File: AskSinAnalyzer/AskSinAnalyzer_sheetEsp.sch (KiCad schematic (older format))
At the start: 14 parts, among them J11 FTDI_ESP, SW11 DIP4, SW12 Flash, SW13 Button, U11 TJCTM24028-SPI, U12 ESP-WROOM-32

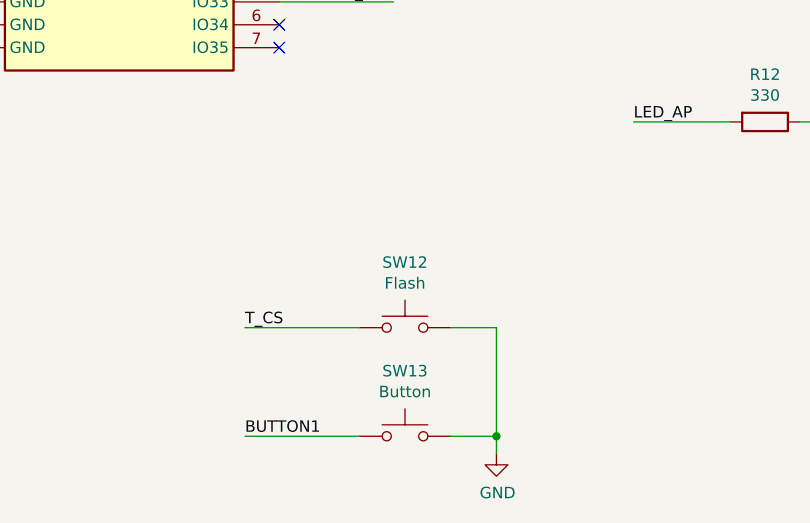
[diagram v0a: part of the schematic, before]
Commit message: PCB update
reference labels moved
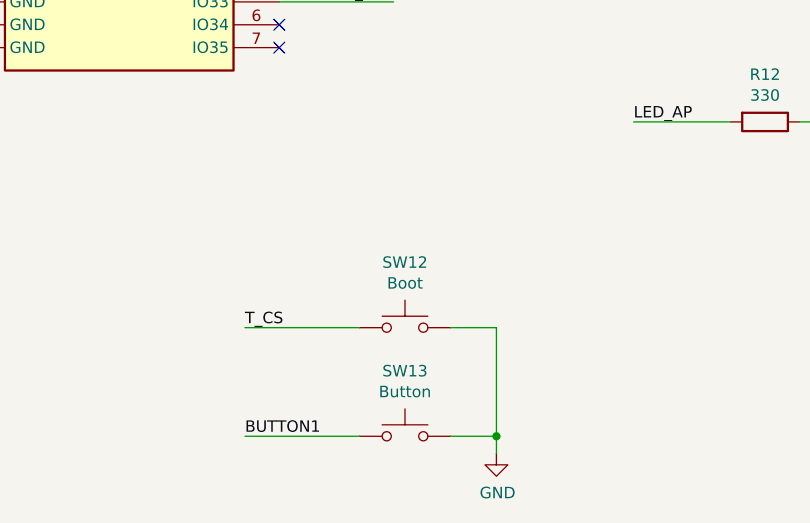
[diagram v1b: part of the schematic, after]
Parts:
- SW12: value Flash -> Boot
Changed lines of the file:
@@
 AR Path="/5D4B4DC0/5D50C20D" Ref="SW12"  Part="1"
 F 0 "SW12" H 5550 6585 50  0000 C CNN
-F 1 "Flash" H 5550 6494 50  0000 C CNN
+F 1 "Boot" H 5550 6494 50  0000 C CNN
 F 2 "Buttons_Switches_THT:SW_PUSH_6mm" H 5550 6500 50  0001 C CNN
 F 3 "~" H 5550 6500 50  0001 C CNN

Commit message: PCB update
pads for ESP made longer
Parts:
- U12: footprint myEspModules:ESP-WROOM-32 -> myEspModules:ESP-WROOM-32_handsoldering
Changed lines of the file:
@@
 F 0 "U12" H 4300 5342 50  0000 C CNN
 F 1 "ESP-WROOM-32" H 4300 5251 50  0000 C CNN
-F 2 "myEspModules:ESP-WROOM-32" H 4300 2375 50  0001 C CNN
+F 2 "myEspModules:ESP-WROOM-32_handsoldering" H 4300 2375 50  0001 C CNN
 F 3 "https://www.espressif.com/sites/default/files/documentation/esp32-wroom-32_datasheet_en.pdf" H 4000 3925 50  0001 C CNN
 	1    4300 3875

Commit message: AskSinAnalyzer PCB V2.0 RC1
added a FTDI FT245 to flash and debug ESP32
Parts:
- added Q11, Q12: BC817, TO_SOT_Packages_SMD:SOT-23_Handsoldering, symbol Transistor_BJT:BC817
- added R13, R14: 10k, Resistors_SMD:R_0805_HandSoldering, symbol Device:R
- added SW14: Reset, Buttons_Switches_THT:SW_PUSH_6mm, symbol Switch:SW_Push
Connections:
- net RX is gone; now on net ESP_RX: J11.3 (TX), U12.34 (RXD0/IO3)
- net TX is gone; now on net ESP_TX: J11.2 (RX), U12.35 (TXD0/IO1)
- net EN: now also Q12.3 (C), SW14.1
- net ESP_RX: no longer U12.27 (IO16)
- net ESP_TX: no longer U12.28 (IO17)
- net GND: now also SW14.2
- net T_CS: now also Q11.3 (C)
- new net: Q11.1 (B), R13.1
- new net: Q12.1 (B), R14.1
- new net ESP_DTR: Q11.2 (E), R14.2
- new net ESP_RTS: Q12.2 (E), R13.2
- new net ESP_RX2: U12.27 (IO16)
- new net ESP_TX2: U12.28 (IO17)
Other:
- moved on the sheet: J11, SW12, SW13
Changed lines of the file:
@@
 Wire Wire Line
 	3450 4975 3450 5075
-Wire Wire Line
-	5000 3025 5500 3025
-Wire Wire Line
-	5500 2825 5000 2825
 Text Label 5500 2825 2    50   ~ 0
 TX
@@
 L myConnectors:FtdiConnector J?
 U 1 1 5D4D5F4D
-P 2625 6450
+P 1200 6475
 AR Path="/5D4D5F4D" Ref="J?"  Part="1"
 AR Path="/5D4B4DC0/5D4D5F4D" Ref="J11"  Part="1"
-F 0 "J11" H 3153 6526 50  0000 L CNN
-F 1 "FTDI_ESP" H 3153 6435 50  0000 L CNN
-F 2 "myPinHeaders:Pin_Header_Straight_1x06_Pitch2.54mm_Tight_Fit" H 2625 6450 50  0001 C CNN
-F 3 "" H 2625 6450 50  0001 C CNN
-	1    2625 6450
-	1    0    0    -1
-$EndComp
-Wire Wire Line
-	2225 6350 2625 6350
+F 0 "J11" H 1728 6551 50  0000 L CNN
+F 1 "FTDI_ESP" H 1728 6460 50  0000 L CNN
+F 2 "myPinHeaders:Pin_Header_Straight_1x06_Pitch2.54mm_Tight_Fit" H 1200 6475 50  0001 C CNN
+F 3 "" H 1200 6475 50  0001 C CNN
+	1    1200 6475
+	1    0    0    -1
+$EndComp
+Wire Wire Line
+	800  6375 1200 6375
 $Comp
 L power:GND #PWR?
 U 1 1 5D4D5F54
-P 2550 6825
+P 1125 6850
 AR Path="/5D4D5F54" Ref="#PWR?"  Part="1"
 AR Path="/5D4B4DC0/5D4D5F54" Ref="#PWR028"  Part="1"
-F 0 "#PWR028" H 2550 6575 50  0001 C CNN
-F 1 "GND" H 2555 6652 50  0000 C CNN
-F 2 "" H 2550 6825 50  0001 C CNN
-F 3 "" H 2550 6825 50  0001 C CNN
-	1    2550 6825
-	1    0    0    -1
-$EndComp
-Wire Wire Line
-	2550 6825 2550 6750
-Wire Wire Line
-	2550 6750 2625 6750
-Wire Wire Line
-	2625 6250 2225 6250
-NoConn ~ 2625 6500
-NoConn ~ 2625 6600
+F 0 "#PWR028" H 1125 6600 50  0001 C CNN
+F 1 "GND" H 1130 6677 50  0000 C CNN
+F 2 "" H 1125 6850 50  0001 C CNN
+F 3 "" H 1125 6850 50  0001 C CNN
+	1    1125 6850
+	1    0    0    -1
+$EndComp
+Wire Wire Line
+	1125 6850 1125 6775
+Wire Wire Line
+	1125 6775 1200 6775
+Wire Wire Line
+	1200 6275 800  6275
+NoConn ~ 1200 6525
+NoConn ~ 1200 6625
 $Comp
 L power:+3.3V #PWR?
 U 1 1 5D4D5F5F
-P 2525 6025
+P 1100 6050
 AR Path="/5D4D5F5F" Ref="#PWR?"  Part="1"
 AR Path="/5D4B4DC0/5D4D5F5F" Ref="#PWR027"  Part="1"
-F 0 "#PWR027" H 2525 5875 50  0001 C CNN
-F 1 "+3.3V" H 2540 6198 50  0000 C CNN
-F 2 "" H 2525 6025 50  0001 C CNN
-F 3 "" H 2525 6025 50  0001 C CNN
-	1    2525 6025
-	1    0    0    -1
-$EndComp
-Wire Wire Line
-	2525 6025 2525 6100
-Wire Wire Line
-	2525 6100 2625 6100
-Text Label 2225 6250 0    50   ~ 0
+F 0 "#PWR027" H 1100 5900 50  0001 C CNN
+F 1 "+3.3V" H 1115 6223 50  0000 C CNN
+F 2 "" H 1100 6050 50  0001 C CNN
+F 3 "" H 1100 6050 50  0001 C CNN
+	1    1100 6050
+	1    0    0    -1
+$EndComp
+Wire Wire Line
+	1100 6050 1100 6125
+Wire Wire Line
+	1100 6125 1200 6125
+Text Label 800  6275 0    50   ~ 0
 TX
-Text Label 2225 6350 0    50   ~ 0
+Text Label 800  6375 0    50   ~ 0
 RX
 $Comp
@@
 L Switch:SW_Push SW?
 U 1 1 5D5050FA
-P 5550 6775
+P 6100 7075
 AR Path="/5D5050FA" Ref="SW?"  Part="1"
 AR Path="/5D4B4DC0/5D5050FA" Ref="SW13"  Part="1"
-F 0 "SW13" H 5550 7060 50  0000 C CNN
-F 1 "Button" H 5550 6969 50  0000 C CNN
-F 2 "Buttons_Switches_THT:SW_PUSH_6mm" H 5550 6975 50  0001 C CNN
-F 3 "~" H 5550 6975 50  0001 C CNN
-	1    5550 6775
-	1    0    0    -1
-$EndComp
-Text Label 4850 6775 0    50   ~ 0
+F 0 "SW13" H 6100 7360 50  0000 C CNN
+F 1 "Button" H 6100 7269 50  0000 C CNN
+F 2 "Buttons_Switches_THT:SW_PUSH_6mm" H 6100 7275 50  0001 C CNN
+F 3 "~" H 6100 7275 50  0001 C CNN
+	1    6100 7075
+	1    0    0    -1
+$EndComp
+Text Label 5400 7075 0    50   ~ 0
 BUTTON1
 Wire Wire Line
-	4850 6775 5350 6775
+	5400 7075 5900 7075
 $Comp
 L power:GND #PWR?
 U 1 1 5D505102
-P 5950 6850
+P 6500 7150
 AR Path="/5D505102" Ref="#PWR?"  Part="1"
 AR Path="/5D4B4DC0/5D505102" Ref="#PWR029"  Part="1"
-F 0 "#PWR029" H 5950 6600 50  0001 C CNN
-F 1 "GND" H 5955 6677 50  0000 C CNN
-F 2 "" H 5950 6850 50  0001 C CNN
-F 3 "" H 5950 6850 50  0001 C CNN
-	1    5950 6850
-	1    0    0    -1
-$EndComp
-Wire Wire Line
-	5950 6850 5950 6775
-Wire Wire Line
-	5950 6775 5750 6775
+F 0 "#PWR029" H 6500 6900 50  0001 C CNN
+F 1 "GND" H 6505 6977 50  0000 C CNN
+F 2 "" H 6500 7150 50  0001 C CNN
+F 3 "" H 6500 7150 50  0001 C CNN
+	1    6500 7150
+	1    0    0    -1
+$EndComp
+Wire Wire Line
+	6500 7150 6500 7075
+Wire Wire Line
+	6500 7075 6300 7075
 Wire Wire Line
 	5000 2725 5500 2725
@@
 L Switch:SW_Push SW?
 U 1 1 5D50C20D
-P 5550 6300
+P 6100 6600
 AR Path="/5D50C20D" Ref="SW?"  Part="1"
 AR Path="/5D4B4DC0/5D50C20D" Ref="SW12"  Part="1"
-F 0 "SW12" H 5550 6585 50  0000 C CNN
-F 1 "Boot" H 5550 6494 50  0000 C CNN
-F 2 "Buttons_Switches_THT:SW_PUSH_6mm" H 5550 6500 50  0001 C CNN
-F 3 "~" H 5550 6500 50  0001 C CNN
-	1    5550 6300
-	1    0    0    -1
-$EndComp
-Wire Wire Line
-	5750 6300 5950 6300
-Wire Wire Line
-	5950 6300 5950 6775
-Connection ~ 5950 6775
-Wire Wire Line
-	5350 6300 4850 6300
-Text Label 4850 6300 0    50   ~ 0
+F 0 "SW12" H 6100 6885 50  0000 C CNN
+F 1 "Boot" H 6100 6794 50  0000 C CNN
+F 2 "Buttons_Switches_THT:SW_PUSH_6mm" H 6100 6800 50  0001 C CNN
+F 3 "~" H 6100 6800 50  0001 C CNN
+	1    6100 6600
+	1    0    0    -1
+$EndComp
+Wire Wire Line
+	6300 6600 6500 6600
+Wire Wire Line
+	6500 6600 6500 7075
+Connection ~ 6500 7075
+Wire Wire Line
+	5900 6600 5400 6600
+Text Label 5400 6600 0    50   ~ 0
 T_CS
 $Comp
@@
 	8675 950  8675 1100
 Text HLabel 5650 3775 2    50   Input ~ 0
-ESP_RX
+ESP_RX2
 Text HLabel 5650 3875 2    50   Input ~ 0
-ESP_TX
+ESP_TX2
 Wire Wire Line
 	10050 3450 9450 3450
@@
 Text Label 3450 3025 0    50   ~ 0
 EN
+$Comp
+L Switch:SW_Push SW?
+U 1 1 5D60F4D4
+P 6100 6125
+AR Path="/5D60F4D4" Ref="SW?"  Part="1"
+AR Path="/5D4B4DC0/5D60F4D4" Ref="SW14"  Part="1"
+F 0 "SW14" H 6100 6410 50  0000 C CNN
+F 1 "Reset" H 6100 6319 50  0000 C CNN
+F 2 "Buttons_Switches_THT:SW_PUSH_6mm" H 6100 6325 50  0001 C CNN
+F 3 "~" H 6100 6325 50  0001 C CNN
+	1    6100 6125
+	1    0    0    -1
+$EndComp
+Wire Wire Line
+	6300 6125 6500 6125
+Wire Wire Line
+	6500 6125 6500 6600
+Connection ~ 6500 6600
+Wire Wire Line
+	5900 6125 5400 6125
+Text Label 5400 6125 0    50   ~ 0
+EN
+$Comp
+L Device:R R?
+U 1 1 5D634714
+P 3275 6150
+AR Path="/5D634714" Ref="R?"  Part="1"
+AR Path="/5D4B4DC0/5D634714" Ref="R13"  Part="1"
+F 0 "R13" V 3068 6150 50  0000 C CNN
+F 1 "10k" V 3159 6150 50  0000 C CNN
+F 2 "Resistors_SMD:R_0805_HandSoldering" V 3205 6150 50  0001 C CNN
+F 3 "~" H 3275 6150 50  0001 C CNN
+	1    3275 6150
+	0    1    1    0
+$EndComp
+$Comp
+L Device:R R?
+U 1 1 5D634C12
+P 3275 6925
+AR Path="/5D634C12" Ref="R?"  Part="1"
+AR Path="/5D4B4DC0/5D634C12" Ref="R14"  Part="1"
+F 0 "R14" V 3068 6925 50  0000 C CNN
+F 1 "10k" V 3159 6925 50  0000 C CNN
+F 2 "Resistors_SMD:R_0805_HandSoldering" V 3205 6925 50  0001 C CNN
+F 3 "~" H 3275 6925 50  0001 C CNN
+	1    3275 6925
+	0    1    1    0
+$EndComp
+Wire Wire Line
+	3425 6925 3500 6925
+Wire Wire Line
+	3425 6150 3500 6150
+Wire Wire Line
+	3125 6150 3000 6150
+Connection ~ 3000 6150
+Wire Wire Line
+	3000 6150 2825 6150
+Wire Wire Line
+	3800 6725 3800 6600
+Wire Wire Line
+	3800 6600 3150 6600
+Wire Wire Line
+	3150 6600 3000 6425
+Wire Wire Line
+	3000 6425 3000 6150
+Wire Wire Line
+	3125 6925 3000 6925
+Wire Wire Line
+	3000 6925 3000 6600
+Wire Wire Line
+	3800 6425 3800 6350
+Wire Wire Line
+	3800 6425 3150 6425
+Wire Wire Line
+	3150 6425 3000 6600
+Wire Wire Line
+	3800 7125 3800 7250
+Wire Wire Line
+	3800 7250 4250 7250
+Text Label 4250 7250 2    50   ~ 0
+EN
+Wire Wire Line
+	3800 5950 3800 5850
+Wire Wire Line
+	3800 5850 4250 5850
+Text Label 4250 5850 2    50   ~ 0
+T_CS
+Text HLabel 2825 6150 0    50   Input ~ 0
+ESP_RTS
+Text HLabel 2825 6925 0    50   Input ~ 0
+ESP_DTR
+Wire Wire Line
+	2825 6925 3000 6925
+Connection ~ 3000 6925
+$Comp
+L Transistor_BJT:BC817 Q11
+U 1 1 5D69CF68
+P 3700 6150
+F 0 "Q11" H 3891 6196 50  0000 L CNN
+F 1 "BC817" H 3891 6105 50  0000 L CNN
+F 2 "TO_SOT_Packages_SMD:SOT-23_Handsoldering" H 3900 6075 50  0001 L CIN
+F 3 "http://www.fairchildsemi.com/ds/BC/BC817.pdf" H 3700 6150 50  0001 L CNN
+	1    3700 6150
+	1    0    0    -1
+$EndComp
+$Comp
+L Transistor_BJT:BC817 Q12
+U 1 1 5D69E995
+P 3700 6925
+F 0 "Q12" H 3891 6879 50  0000 L CNN
+F 1 "BC817" H 3891 6970 50  0000 L CNN
+F 2 "TO_SOT_Packages_SMD:SOT-23_Handsoldering" H 3900 6850 50  0001 L CIN
+F 3 "http://www.fairchildsemi.com/ds/BC/BC817.pdf" H 3700 6925 50  0001 L CNN
+	1    3700 6925
+	1    0    0    1
+$EndComp
+Text HLabel 5650 3025 2    50   Input ~ 0
+ESP_RX
+Text HLabel 5650 2825 2    50   Input ~ 0
+ESP_TX
+Wire Wire Line
+	5000 3025 5650 3025
+Wire Wire Line
+	5000 2825 5650 2825
 $EndSCHEMATC

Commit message: AskSinAnalyzer PCB V2.0
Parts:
- added R15: 10k, Resistors_SMD:R_0805_HandSoldering, symbol Device:R
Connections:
- net +3V3: now also R15.1
- net T_CS: now also R15.2
- net SW_DETAIL renamed SW1_DETAIL
- net SW_LINES renamed SW3_LINES
- net SW_ONLINE renamed SW2_ONLINE
- net SW_UNUSED renamed SW4_UNUSED
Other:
- moved on the sheet: SW12, SW14
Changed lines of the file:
@@
 NoConn ~ 5000 4975
 NoConn ~ 5000 4275
-NoConn ~ 5000 4175
 NoConn ~ 3600 3625
 NoConn ~ 3600 3725
 NoConn ~ 3600 3825
 Text Label 5500 3375 2    50   ~ 0
-SW_DETAIL
+SW1_DETAIL
 Wire Wire Line
 	5500 3375 5000 3375
 Text Label 5500 3475 2    50   ~ 0
-SW_LINES
+SW3_LINES
 Text Label 5500 3575 2    50   ~ 0
-SW_ONLINE
+SW2_ONLINE
 Text Label 5500 3675 2    50   ~ 0
 BUTTON1
@@
 	5000 3125 5500 3125
 Text Label 5500 3125 2    50   ~ 0
-SW_UNUSED
+SW4_UNUSED
 $Comp
 L power:GND #PWR?
@@
 	9075 5350 8675 5350
 Text Label 8675 5350 0    50   ~ 0
-SW_DETAIL
+SW1_DETAIL
 Text Label 8675 5450 0    50   ~ 0
-SW_ONLINE
+SW2_ONLINE
 Text Label 8675 5550 0    50   ~ 0
-SW_LINES
+SW3_LINES
 Wire Wire Line
 	8675 5550 9075 5550
@@
 	9075 5650 8675 5650
 Text Label 8675 5650 0    50   ~ 0
-SW_UNUSED
+SW4_UNUSED
 Wire Wire Line
 	9675 5650 9775 5650
@@
 	6500 7075 6300 7075
 Wire Wire Line
-	5000 2725 5500 2725
+	5000 2725 5250 2725
 Text Label 5500 2725 2    50   ~ 0
 T_CS
@@
 L Switch:SW_Push SW?
 U 1 1 5D50C20D
-P 6100 6600
+P 6100 6125
 AR Path="/5D50C20D" Ref="SW?"  Part="1"
 AR Path="/5D4B4DC0/5D50C20D" Ref="SW12"  Part="1"
-F 0 "SW12" H 6100 6885 50  0000 C CNN
-F 1 "Boot" H 6100 6794 50  0000 C CNN
-F 2 "Buttons_Switches_THT:SW_PUSH_6mm" H 6100 6800 50  0001 C CNN
-F 3 "~" H 6100 6800 50  0001 C CNN
-	1    6100 6600
-	1    0    0    -1
-$EndComp
-Wire Wire Line
-	6300 6600 6500 6600
-Wire Wire Line
-	6500 6600 6500 7075
+F 0 "SW12" H 6100 6410 50  0000 C CNN
+F 1 "Boot" H 6100 6319 50  0000 C CNN
+F 2 "Buttons_Switches_THT:SW_PUSH_6mm" H 6100 6325 50  0001 C CNN
+F 3 "~" H 6100 6325 50  0001 C CNN
+	1    6100 6125
+	1    0    0    -1
+$EndComp
+Wire Wire Line
+	6300 6125 6500 6125
 Connection ~ 6500 7075
-Wire Wire Line
-	5900 6600 5400 6600
-Text Label 5400 6600 0    50   ~ 0
+Text Label 5400 6125 0    50   ~ 0
 T_CS
 $Comp
@@
 L Switch:SW_Push SW?
 U 1 1 5D60F4D4
-P 6100 6125
+P 6100 6625
 AR Path="/5D60F4D4" Ref="SW?"  Part="1"
 AR Path="/5D4B4DC0/5D60F4D4" Ref="SW14"  Part="1"
-F 0 "SW14" H 6100 6410 50  0000 C CNN
-F 1 "Reset" H 6100 6319 50  0000 C CNN
-F 2 "Buttons_Switches_THT:SW_PUSH_6mm" H 6100 6325 50  0001 C CNN
-F 3 "~" H 6100 6325 50  0001 C CNN
-	1    6100 6125
-	1    0    0    -1
-$EndComp
-Wire Wire Line
-	6300 6125 6500 6125
-Wire Wire Line
-	6500 6125 6500 6600
-Connection ~ 6500 6600
-Wire Wire Line
-	5900 6125 5400 6125
-Text Label 5400 6125 0    50   ~ 0
+F 0 "SW14" H 6100 6910 50  0000 C CNN
+F 1 "Reset" H 6100 6819 50  0000 C CNN
+F 2 "Buttons_Switches_THT:SW_PUSH_6mm" H 6100 6825 50  0001 C CNN
+F 3 "~" H 6100 6825 50  0001 C CNN
+	1    6100 6625
+	1    0    0    -1
+$EndComp
+Wire Wire Line
+	6300 6625 6500 6625
+Wire Wire Line
+	5900 6625 5400 6625
+Text Label 5400 6625 0    50   ~ 0
 EN
 $Comp
@@
 Text HLabel 2825 6150 0    50   Input ~ 0
 ESP_RTS
-Text HLabel 2825 6925 0    50   Input ~ 0
-ESP_DTR
-Wire Wire Line
-	2825 6925 3000 6925
-Connection ~ 3000 6925
 $Comp
 L Transistor_BJT:BC817 Q11
@@
 Wire Wire Line
 	5000 2825 5650 2825
+NoConn ~ 5000 4175
+$Comp
+L Device:R R15
+U 1 1 5D7568C8
+P 5250 2475
+F 0 "R15" H 5320 2521 50  0000 L CNN
+F 1 "10k" H 5320 2430 50  0000 L CNN
+F 2 "Resistors_SMD:R_0805_HandSoldering" V 5180 2475 50  0001 C CNN
+F 3 "~" H 5250 2475 50  0001 C CNN
+	1    5250 2475
+	1    0    0    -1
+$EndComp
+Wire Wire Line
+	6500 6125 6500 6625
+Connection ~ 6500 6625
+Wire Wire Line
+	6500 6625 6500 7075
+Wire Wire Line
+	5250 2625 5250 2725
+$Comp
+L power:+3.3V #PWR?
+U 1 1 5D77D83D
+P 5250 2250
+AR Path="/5D77D83D" Ref="#PWR?"  Part="1"
+AR Path="/5D4B4DC0/5D77D83D" Ref="#PWR030"  Part="1"
+F 0 "#PWR030" H 5250 2100 50  0001 C CNN
+F 1 "+3.3V" H 5265 2423 50  0000 C CNN
+F 2 "" H 5250 2250 50  0001 C CNN
+F 3 "" H 5250 2250 50  0001 C CNN
+	1    5250 2250
+	1    0    0    -1
+$EndComp
+Wire Wire Line
+	5250 2250 5250 2325
+Connection ~ 5250 2725
+Wire Wire Line
+	5250 2725 5500 2725
+Wire Wire Line
+	5400 6125 5900 6125
+Text HLabel 2825 6925 0    50   Input ~ 0
+ESP_DTR
+Wire Wire Line
+	2825 6925 3000 6925
+Connection ~ 3000 6925
 $EndSCHEMATC

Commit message: add production data to AskSinAnalyzer PCB
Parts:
- C11, C13: LCSC (none) -> C15850
- C12, C14, C15: LCSC (none) -> C49678
- J11, LED11, SW11, SW12, SW13, SW14, U11, U12: LCSC (none) -> -
- Q11, Q12: LCSC (none) -> C2137; Option (none) -> 3_USB_debugging
- R11, R15: LCSC (none) -> C17414
- R12: LCSC (none) -> C17630
- R13, R14: LCSC (none) -> C17414; Option (none) -> 3_USB_debugging
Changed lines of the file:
@@
 F 2 "myDisplays:TJCTM24028-SPI" H 8650 2450 50  0001 C CNN
 F 3 "http://pan.baidu.com/s/11Y990" H 8000 3650 50  0001 C CNN
+F 4 "-" H 8650 3150 50  0001 C CNN "LCSC"
 	1    8650 3150
 	1    0    0    -1
@@
 F 2 "myEspModules:ESP-WROOM-32_handsoldering" H 4300 2375 50  0001 C CNN
 F 3 "https://www.espressif.com/sites/default/files/documentation/esp32-wroom-32_datasheet_en.pdf" H 4000 3925 50  0001 C CNN
+F 4 "-" H 4300 3875 50  0001 C CNN "LCSC"
 	1    4300 3875
 	1    0    0    -1
@@
 F 2 "myPinHeaders:Pin_Header_Straight_1x06_Pitch2.54mm_Tight_Fit" H 1200 6475 50  0001 C CNN
 F 3 "" H 1200 6475 50  0001 C CNN
+F 4 "-" H 1200 6475 50  0001 C CNN "LCSC"
 	1    1200 6475
 	1    0    0    -1
@@
 F 2 "Resistors_SMD:R_0805_HandSoldering" V 7055 5400 50  0001 C CNN
 F 3 "~" H 7125 5400 50  0001 C CNN
+F 4 "C17630" H 7125 5400 50  0001 C CNN "LCSC"
 	1    7125 5400
 	0    1    1    0
@@
 F 2 "LEDs:LED_D3.0mm_Horizontal_O3.81mm_Z6.0mm" H 7550 5400 50  0001 C CNN
 F 3 "~" H 7550 5400 50  0001 C CNN
+F 4 "-" H 7550 5400 50  0001 C CNN "LCSC"
 	1    7550 5400
 	-1   0    0    1
@@
 F 2 "Buttons_Switches_THT:SW_DIP_x4_W7.62mm_Slide" H 9375 5550 50  0001 C CNN
 F 3 "~" H 9375 5550 50  0001 C CNN
+F 4 "-" H 9375 5550 50  0001 C CNN "LCSC"
 	1    9375 5550
 	1    0    0    -1
@@
 F 2 "Buttons_Switches_THT:SW_PUSH_6mm" H 6100 7275 50  0001 C CNN
 F 3 "~" H 6100 7275 50  0001 C CNN
+F 4 "-" H 6100 7075 50  0001 C CNN "LCSC"
 	1    6100 7075
 	1    0    0    -1
@@
 F 2 "Buttons_Switches_THT:SW_PUSH_6mm" H 6100 6325 50  0001 C CNN
 F 3 "~" H 6100 6325 50  0001 C CNN
+F 4 "-" H 6100 6125 50  0001 C CNN "LCSC"
 	1    6100 6125
 	1    0    0    -1
@@
 F 2 "Resistors_SMD:R_0805_HandSoldering" V 2805 2775 50  0001 C CNN
 F 3 "~" H 2875 2775 50  0001 C CNN
+F 4 "C17414" H 2875 2775 50  0001 C CNN "LCSC"
 	1    2875 2775
 	1    0    0    -1
@@
 F 2 "Capacitors_SMD:C_0805_HandSoldering" H 2913 3125 50  0001 C CNN
 F 3 "~" H 2875 3275 50  0001 C CNN
+F 4 "C49678" H 2875 3275 50  0001 C CNN "LCSC"
 	1    2875 3275
 	1    0    0    -1
@@
 F 2 "Capacitors_SMD:C_0805_HandSoldering" H 4538 1125 50  0001 C CNN
 F 3 "~" H 4500 1275 50  0001 C CNN
+F 4 "C49678" H 4500 1275 50  0001 C CNN "LCSC"
 	1    4500 1275
 	1    0    0    -1
@@
 F 2 "Capacitors_SMD:C_0805_HandSoldering" H 4088 1125 50  0001 C CNN
 F 3 "~" H 4050 1275 50  0001 C CNN
+F 4 "C15850" H 4050 1275 50  0001 C CNN "LCSC"
 	1    4050 1275
 	1    0    0    -1
@@
 F 2 "Capacitors_SMD:C_0805_HandSoldering" H 8713 1100 50  0001 C CNN
 F 3 "~" H 8675 1250 50  0001 C CNN
+F 4 "C49678" H 8675 1250 50  0001 C CNN "LCSC"
 	1    8675 1250
 	1    0    0    -1
@@
 F 2 "Capacitors_SMD:C_0805_HandSoldering" H 8263 1100 50  0001 C CNN
 F 3 "~" H 8225 1250 50  0001 C CNN
+F 4 "C15850" H 8225 1250 50  0001 C CNN "LCSC"
 	1    8225 1250
 	1    0    0    -1
@@
 F 2 "Buttons_Switches_THT:SW_PUSH_6mm" H 6100 6825 50  0001 C CNN
 F 3 "~" H 6100 6825 50  0001 C CNN
+F 4 "-" H 6100 6625 50  0001 C CNN "LCSC"
 	1    6100 6625
 	1    0    0    -1
@@
 F 2 "Resistors_SMD:R_0805_HandSoldering" V 3205 6150 50  0001 C CNN
 F 3 "~" H 3275 6150 50  0001 C CNN
+F 4 "C17414" H 3275 6150 50  0001 C CNN "LCSC"
+F 5 "3_USB_debugging" H 3275 6150 50  0001 C CNN "Option"
 	1    3275 6150
 	0    1    1    0
@@
 F 2 "Resistors_SMD:R_0805_HandSoldering" V 3205 6925 50  0001 C CNN
 F 3 "~" H 3275 6925 50  0001 C CNN
+F 4 "C17414" H 3275 6925 50  0001 C CNN "LCSC"
+F 5 "3_USB_debugging" H 3275 6925 50  0001 C CNN "Option"
 	1    3275 6925
 	0    1    1    0
@@
 F 2 "TO_SOT_Packages_SMD:SOT-23_Handsoldering" H 3900 6075 50  0001 L CIN
 F 3 "http://www.fairchildsemi.com/ds/BC/BC817.pdf" H 3700 6150 50  0001 L CNN
+F 4 "C2137" H 3700 6150 50  0001 C CNN "LCSC"
+F 5 "3_USB_debugging" H 3700 6150 50  0001 C CNN "Option"
 	1    3700 6150
 	1    0    0    -1
@@
 F 2 "TO_SOT_Packages_SMD:SOT-23_Handsoldering" H 3900 6850 50  0001 L CIN
 F 3 "http://www.fairchildsemi.com/ds/BC/BC817.pdf" H 3700 6925 50  0001 L CNN
+F 4 "C2137" H 3700 6925 50  0001 C CNN "LCSC"
+F 5 "3_USB_debugging" H 3700 6925 50  0001 C CNN "Option"
 	1    3700 6925
 	1    0    0    1
@@
 F 2 "Resistors_SMD:R_0805_HandSoldering" V 5180 2475 50  0001 C CNN
 F 3 "~" H 5250 2475 50  0001 C CNN
+F 4 "C17414" H 5250 2475 50  0001 C CNN "LCSC"
 	1    5250 2475
 	1    0    0    -1
